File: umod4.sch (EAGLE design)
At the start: 75 parts, among them IC3 27C256-FEED-THRU, J1 DMSAT-SF-PEJ, J2 10118194-0001LF, J3 BM04B-SRSS-TB, J4 BM04B-SRSS-TB, J5 C160394/JST BM08B-SRSS, M1 RPi Pico W, M2 Generic single-sided NEO-8, Q1 C10487/SI2301CDS, Q2 C2150/SS8050, U1 C113281/74LVC541, U2 C6091/74LVC4245, U3 C113281/74LVC541, U4 C2040/RP2040, U5 C97521/W25Q128JVSIQ, U6 C10428/74LVC2G04, U7 C10428/74LVC2G04, Y1 C9002/12MHz

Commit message: Updates to README, Changelist, and design
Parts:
- removed JP4: NC, SparkFun-Jumpers:JUMPER-SMT_2_NC_TRACE_NO-SILK
- removed R17: C25744/10K, SparkFun-03-01-2010:RESISTOR0402-RES
- removed TP2: (no value), robins-v7:TEST-POINT-1035
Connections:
- removed net !ADDR_EN!: M1.GP21, R17.2, U1.!OE2, U3.!OE2
- removed net N$16: JP4.2, TP2.TP, U4.GPIO28_ADC2
- net !RESET!_HC11_OUT: now also U4.GPIO28_ADC2; no longer JP4.1
- net +3V3: no longer R17.1
- net GND: now also U1.!OE2, U3.!OE2
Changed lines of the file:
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@@
 <part name="+3V16" library="supply1" deviceset="+3V3" device=""/>
 <part name="V17" library="supply2" deviceset="GND" device=""/>
-<part name="TP2" library="robins-v7" deviceset="TEST-POINT" device="-1035"/>
 <part name="TP3" library="robins-v7" deviceset="TEST-POINT" device="-1035"/>
 <part name="V18" library="supply2" deviceset="GND" device=""/>
@@
 <part name="S2" library="robins-v7" deviceset="SWITCH" device="-TAC-5.2MM"/>
 <part name="V37" library="supply2" deviceset="GND" device=""/>
-<part name="R17" library="SparkFun-03-01-2010" deviceset="RESISTOR" device="0402-RES" value="C25744/10K">
-<attribute name="LCSC_PART" value="C25744"/>
-</part>
-<part name="+3V22" library="supply1" deviceset="+3V3" device=""/>
 <part name="JP2" library="pinhead" deviceset="PINHD-1X2" device=""/>
 <part name="+3V23" library="supply1" deviceset="+3V3" device=""/>
@@
 </part>
 <part name="V39" library="supply2" deviceset="GND" device=""/>
-<part name="JP4" library="SparkFun-Jumpers" deviceset="JUMPER-SMT_2_NC_TRACE" device="_NO-SILK" value="NC"/>
+<part name="V28" library="supply2" deviceset="GND" device=""/>
+<part name="V40" library="supply2" deviceset="GND" device=""/>
 </parts>
 <sheets>
@@
 <instance part="V32" gate="GND" x="147.32" y="46.99" rot="MR270"/>
 <instance part="JP3" gate="G$1" x="142.24" y="52.07" rot="R90"/>
-<instance part="R17" gate="G$1" x="38.1" y="50.8" smashed="yes">
-<attribute name="NAME" x="34.29" y="52.2986" size="1.778" layer="95"/>
-<attribute name="VALUE" x="31.75" y="47.498" size="1.778" layer="96"/>
-<attribute name="LCSC_PART" x="25.4" y="45.72" size="1.27" layer="96" display="both"/>
-</instance>
-<instance part="+3V22" gate="G$1" x="30.48" y="55.88"/>
 <instance part="R18" gate="G$1" x="96.52" y="63.5" rot="R180">
 <attribute name="LCSC_PART" x="104.14" y="68.58" size="1.27" layer="96" rot="R180" display="both"/>
 </instance>
+<instance part="V28" gate="GND" x="45.72" y="55.88" rot="MR0"/>
+<instance part="V40" gate="GND" x="45.72" y="93.98" rot="MR0"/>
 </instances>
 <busses>
@@
 <pinref part="JP3" gate="G$1" pin="1"/>
 </segment>
+<segment>
+<pinref part="U1" gate="G$1" pin="!OE2"/>
+<wire x1="48.26" y1="99.06" x2="45.72" y2="99.06" width="0.1524" layer="91"/>
+<pinref part="V40" gate="GND" pin="GND"/>
+<wire x1="45.72" y1="96.52" x2="45.72" y2="99.06" width="0.1524" layer="91"/>
+</segment>
+<segment>
+<pinref part="V28" gate="GND" pin="GND"/>
+<wire x1="45.72" y1="58.42" x2="45.72" y2="60.96" width="0.1524" layer="91"/>
+<pinref part="U3" gate="G$1" pin="!OE2"/>
+<wire x1="45.72" y1="60.96" x2="48.26" y2="60.96" width="0.1524" layer="91"/>
+</segment>
 </net>
 <net name="+3V3" class="0">
@@
 <junction x="205.74" y="81.28"/>
 <pinref part="+3V17" gate="G$1" pin="+3V3"/>
-</segment>
-<segment>
-<pinref part="R17" gate="G$1" pin="1"/>
-<wire x1="33.02" y1="50.8" x2="30.48" y2="50.8" width="0.1524" layer="91"/>
-<pinref part="+3V22" gate="G$1" pin="+3V3"/>
-<wire x1="30.48" y1="50.8" x2="30.48" y2="53.34" width="0.1524" layer="91"/>
 </segment>
 </net>
@@
 <wire x1="170.18" y1="78.74" x2="180.34" y2="78.74" width="0.1524" layer="91"/>
 <label x="180.34" y="78.74" size="1.27" layer="95" xref="yes"/>
-</segment>
-</net>
-<net name="!ADDR_EN!" class="0">
-<segment>
-<pinref part="U3" gate="G$1" pin="!OE2"/>
-<wire x1="48.26" y1="60.96" x2="45.72" y2="60.96" width="0.1524" layer="91"/>
-<pinref part="U1" gate="G$1" pin="!OE2"/>
-<wire x1="45.72" y1="60.96" x2="38.1" y2="60.96" width="0.1524" layer="91"/>
-<wire x1="48.26" y1="99.06" x2="45.72" y2="99.06" width="0.1524" layer="91"/>
-<wire x1="45.72" y1="99.06" x2="45.72" y2="60.96" width="0.1524" layer="91"/>
-<junction x="45.72" y="60.96"/>
-<label x="38.1" y="60.96" size="1.27" layer="95" rot="R180" xref="yes"/>
-<pinref part="R17" gate="G$1" pin="2"/>
-<wire x1="43.18" y1="50.8" x2="45.72" y2="50.8" width="0.1524" layer="91"/>
-<wire x1="45.72" y1="50.8" x2="45.72" y2="60.96" width="0.1524" layer="91"/>
 </segment>
 </net>
@@
 <attribute name="LCSC_PART" x="58.42" y="12.7" size="1.27" layer="96" rot="R90" display="both"/>
 </instance>
-<instance part="TP2" gate="G$1" x="200.66" y="63.5"/>
 <instance part="TP3" gate="G$1" x="15.24" y="60.96"/>
 <instance part="V18" gate="GND" x="15.24" y="55.88" rot="MR0"/>
@@
 </instance>
 <instance part="V39" gate="GND" x="63.5" y="127" rot="MR270"/>
-<instance part="JP4" gate="G$1" x="208.28" y="60.96" rot="R180"/>
 </instances>
 <busses>
@@
 </segment>
 </net>
-<net name="N$16" class="0">
-<segment>
-<pinref part="U4" gate="G$1" pin="GPIO28_ADC2"/>
-<wire x1="160.02" y1="60.96" x2="200.66" y2="60.96" width="0.1524" layer="91"/>
-<wire x1="200.66" y1="60.96" x2="200.66" y2="63.5" width="0.1524" layer="91"/>
-<pinref part="TP2" gate="G$1" pin="TP"/>
-<wire x1="200.66" y1="60.96" x2="203.2" y2="60.96" width="0.1524" layer="91"/>
-<junction x="200.66" y="60.96"/>
-<pinref part="JP4" gate="G$1" pin="2"/>
-</segment>
-</net>
 <net name="N$13" class="0">
 <segment>
@@
 <net name="!RESET!_HC11_OUT" class="0">
 <segment>
-<pinref part="JP4" gate="G$1" pin="1"/>
-<wire x1="213.36" y1="60.96" x2="218.44" y2="60.96" width="0.1524" layer="91"/>
-<label x="218.44" y="60.96" size="1.27" layer="95" xref="yes"/>
+<label x="170.18" y="60.96" size="1.27" layer="95" xref="yes"/>
+<pinref part="U4" gate="G$1" pin="GPIO28_ADC2"/>
+<wire x1="170.18" y1="60.96" x2="160.02" y2="60.96" width="0.1524" layer="91"/>
 </segment>
 </net>
@@
 </segment>
 </net>
-<net name="!ADDR_EN!" class="0">
-<segment>
-<pinref part="M1" gate="G$1" pin="GP21"/>
-<wire x1="180.34" y1="124.46" x2="195.58" y2="124.46" width="0.1524" layer="91"/>
-<label x="195.58" y="124.46" size="1.27" layer="95" xref="yes"/>
-</segment>
-</net>

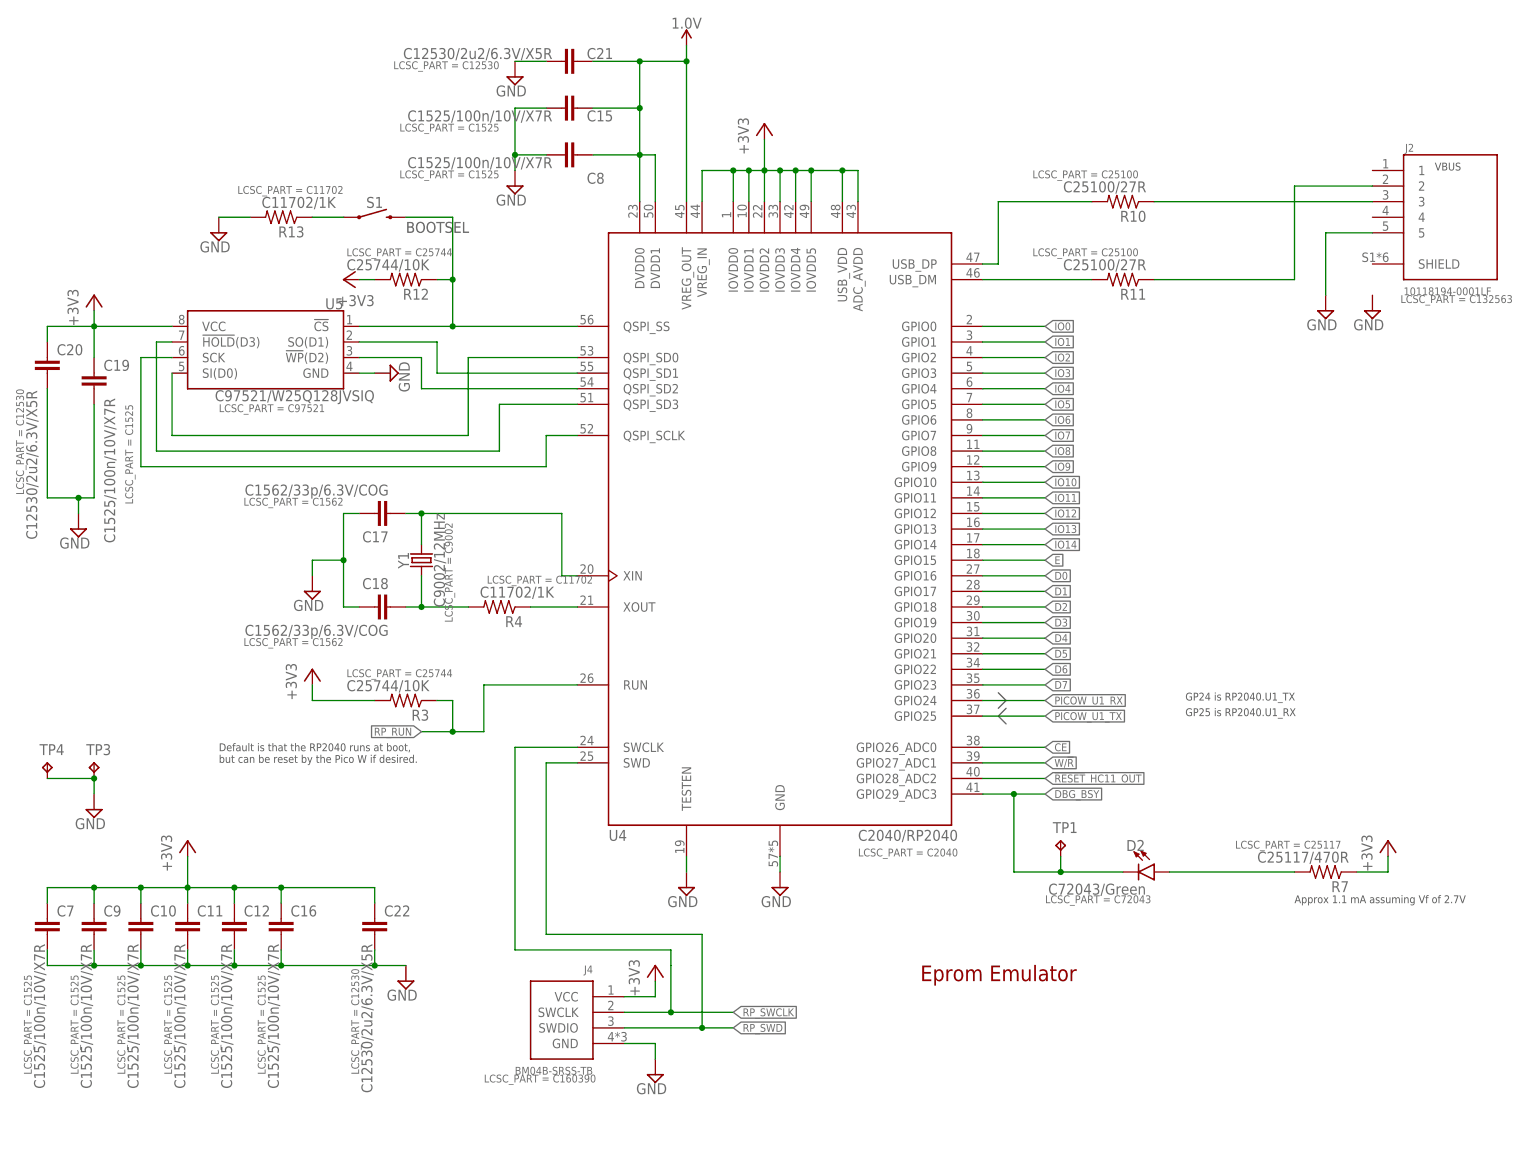
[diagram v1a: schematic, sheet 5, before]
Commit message: New: 10-pin SWD, WS2812-2020, TestPlan doc
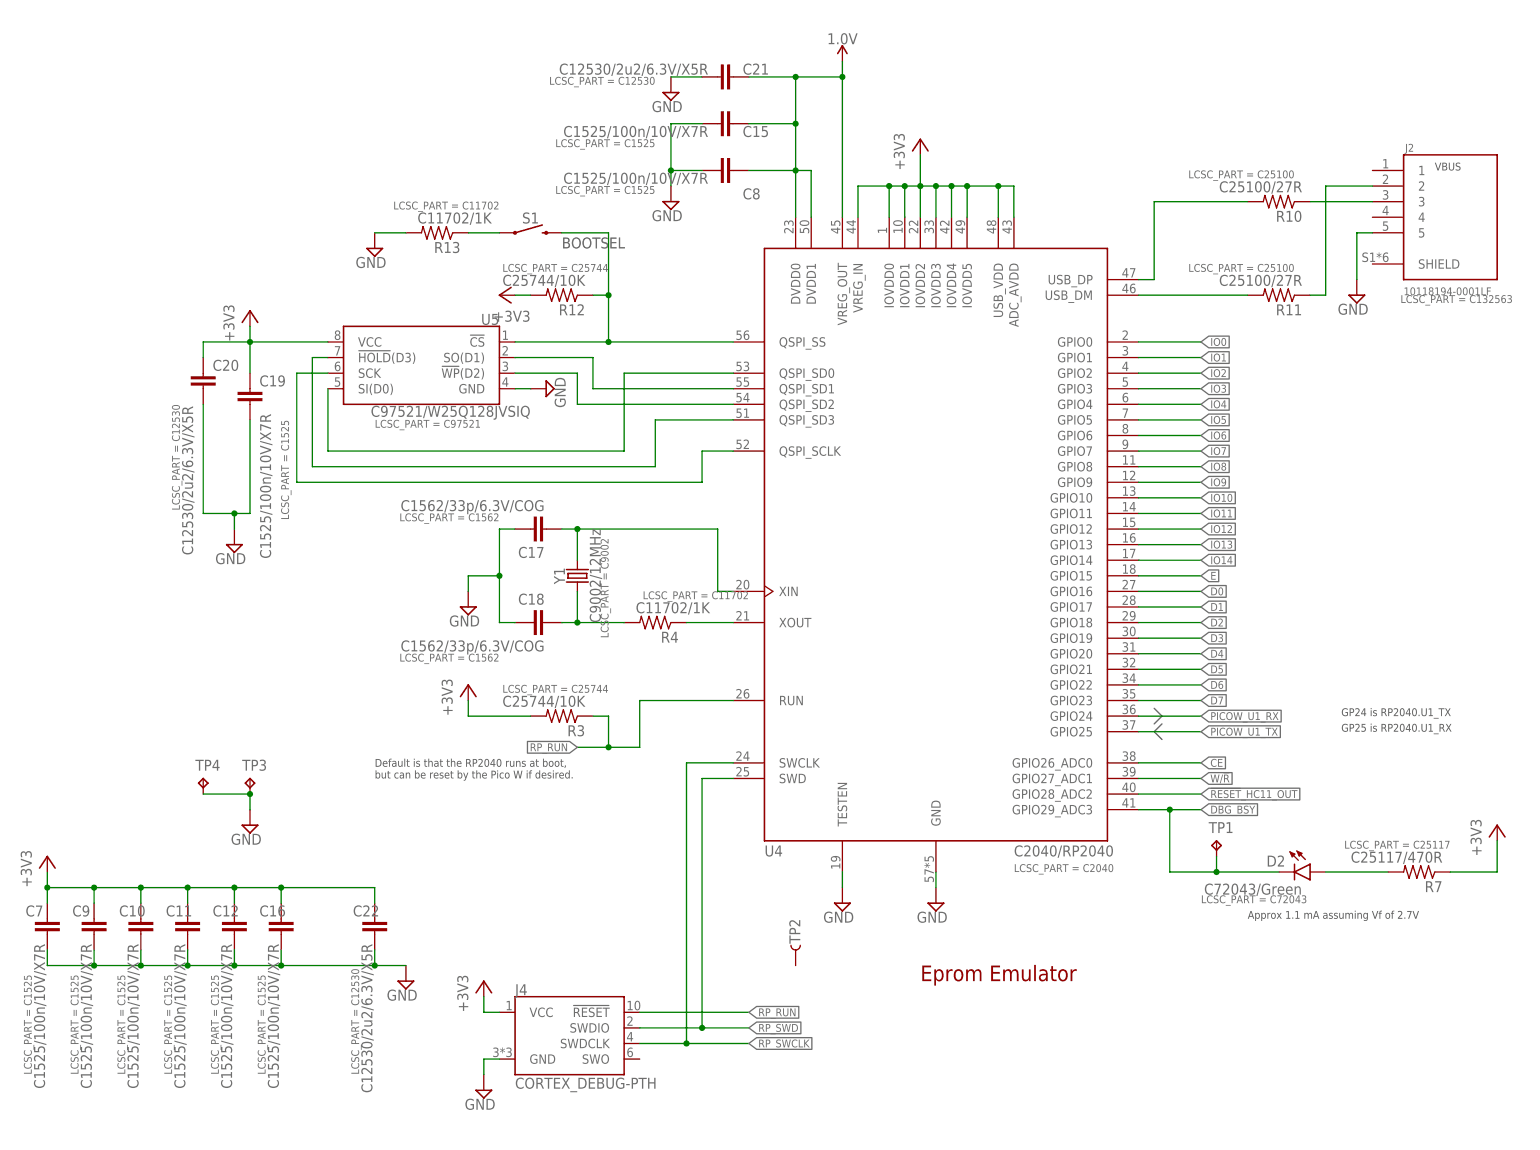
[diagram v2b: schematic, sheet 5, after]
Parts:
- removed J3: BM04B-SRSS-TB, robins-v7:PICO-DEBUG-JST-SH-VERT
- added J6: CORTEX_DEBUG-PTH, robins-v7:CORTEX_DEBUG-PTH
- added TP2: TEST-POINT3X5, SparkFun-Connectors:TEST-POINT3X5
- J4: value BM04B-SRSS-TB -> CORTEX_DEBUG-PTH; device robins-v7:PICO-DEBUG-JST-SH-VERT -> robins-v7:CORTEX_DEBUG-PTH; LCSC_PART C160390 -> (none)
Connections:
- removed net !RESET!_HC11_IN: M1.GP14
- removed net N$19: J3.SWDIO, M1.SWDIO
- removed net N$3: J3.SWCLK, M1.SWCLK
- new net SPARE3: M1.GP21
- new net WP_RUN: J6.!RESET, M1.RUN
- new net WP_SDIO: J6.SWDIO, M1.SWDIO
- new net WP_SWCLK: J6.SWDCLK, M1.SWCLK
- net +3V3: now also J6.VCC; no longer J3.VCC, M1.RUN
- net GND: now also J6.GND; no longer J3.GND
- net RP_RUN: now also J4.!RESET
- net RP_SWCLK: now also J4.SWDCLK; no longer J4.SWCLK
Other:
- note added: "LCD_BKLT"
- note added: "LCD_CS"
- note added: "LCD_DC"
- note added: "LCD_GND"
- note added: "LCD_SCK"
- note added: "LCD_SDA"
- note added: "LCD_VCC"
- moved on the sheet: C15, C17, C18, C19, C20, C21, C8, D2, R10, R11, R12, R13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
